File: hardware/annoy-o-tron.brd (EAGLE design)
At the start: 100 x 78.2 mm, 22 parts, among them J1 USB-MICROB, J2 DM3AT-SF-PEJM5, U1 ATMEGA32-16AU, U2 TPS62203DBVT

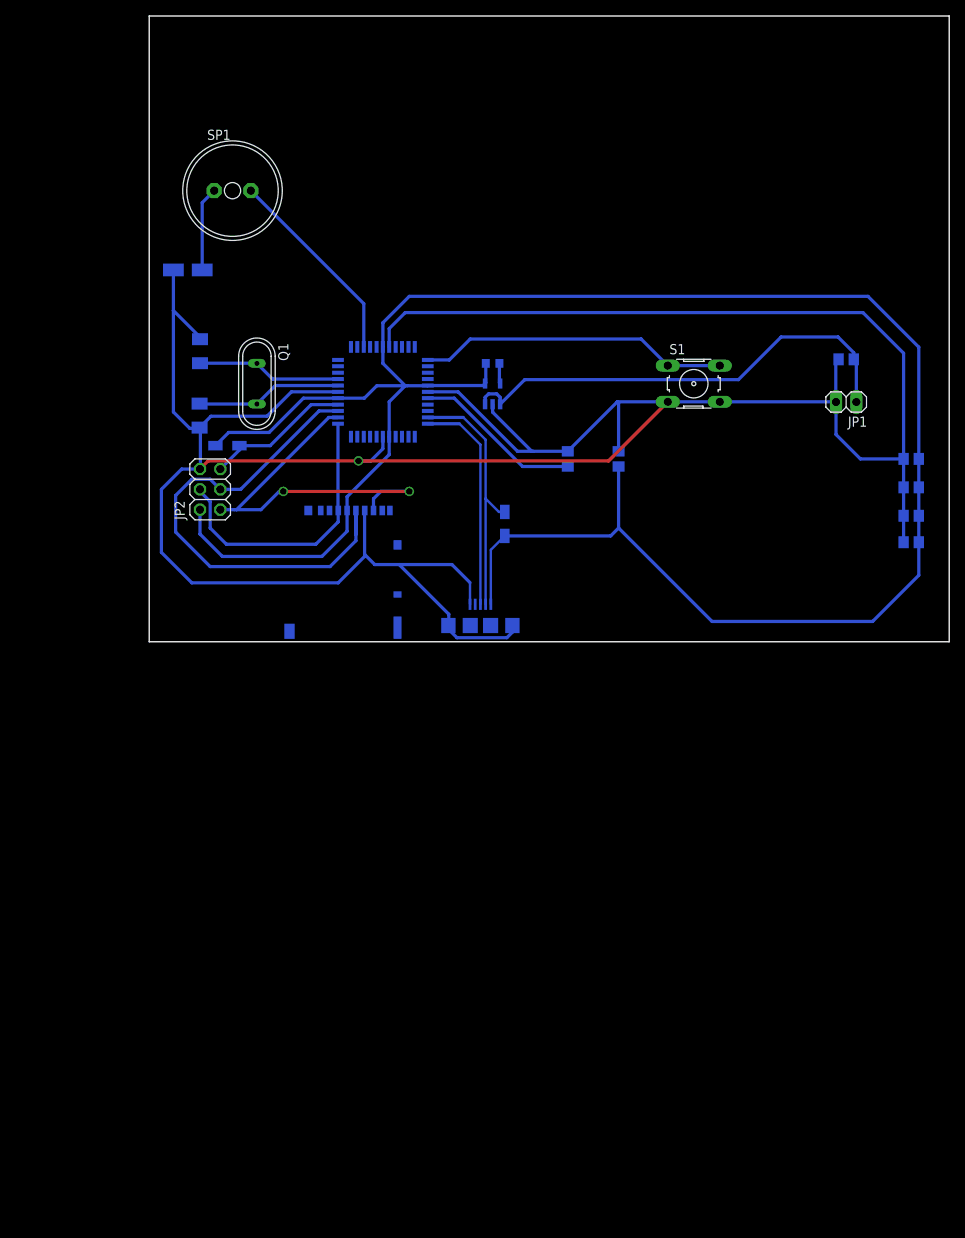
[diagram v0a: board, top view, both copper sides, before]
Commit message: Replaced ATmega32-16 with ATmega328P. Replace TPS62201 with TPS61201, schematic stil unfinished.
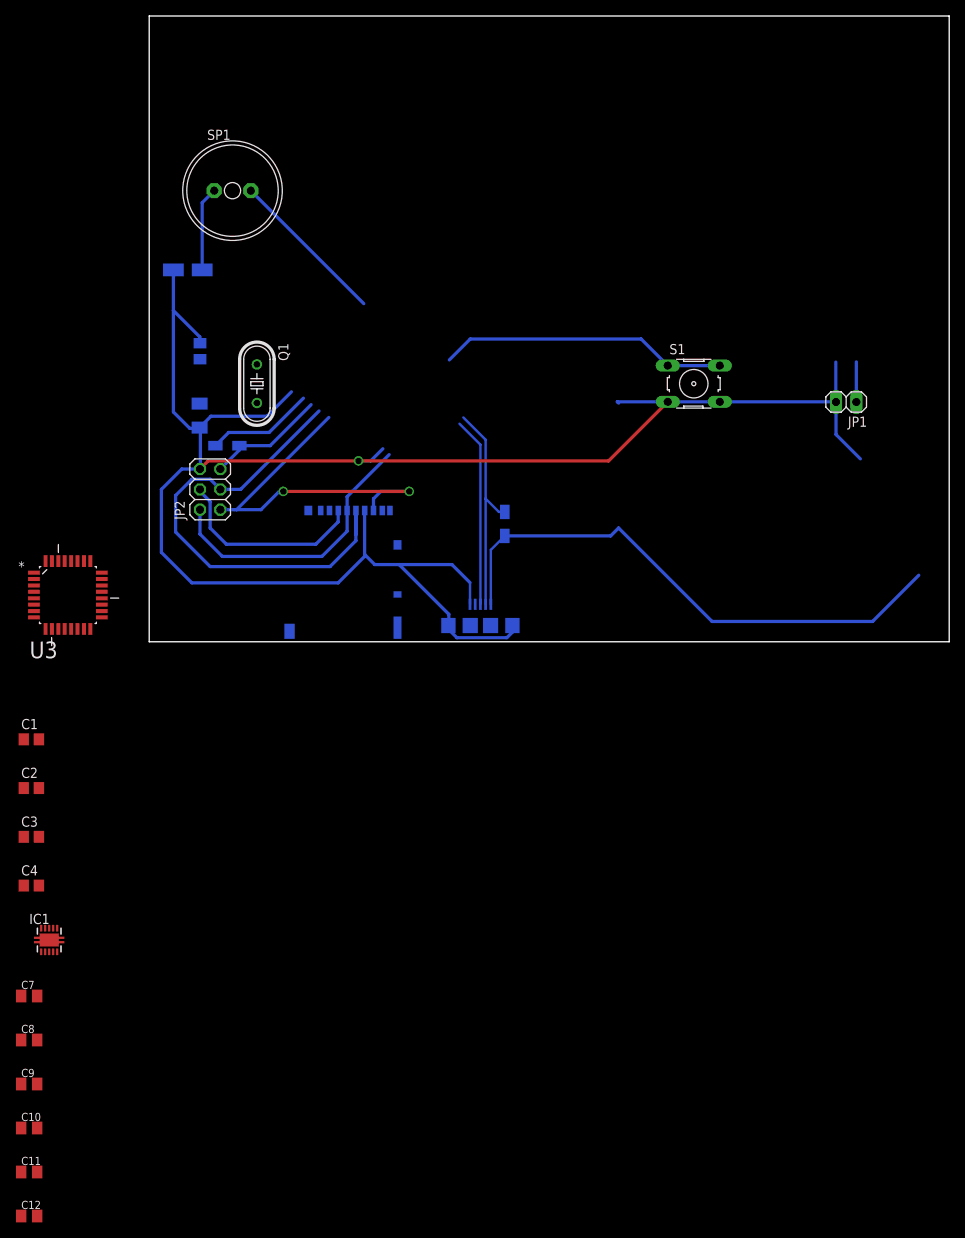
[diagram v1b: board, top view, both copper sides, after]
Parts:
- removed L1: 10uH, rcl:R0603
- removed U1: ATMEGA32-16AU, annoy-o-library:QFP80P1200X1200X120-44N
- removed U2: TPS62203DBVT, annoy-o-library:SOT95P280X145-5N
- added C11: 1uF, resistor:C0805K
- added C12: 100nF, resistor:C0805K
- added C44: 100uF, resistor:153CLV-0405
- added IC1: TPS61201, texas:S-PDSO-N10
- added U3: ATMEGA328P-AU, tudor:QFP80P900X900X120-32N
- C1: value 4.7uF -> 100nF
- C10, C7: value 100nF -> 10uF; device rcl:C0805 -> resistor:C0805K
- C2: value 10uF -> 100nF
- C4: value 100uF -> 100nF; device resistor:153CLV-0405 -> rcl:C0805
- C6: device resistor:C1206K -> resistor:C0805K
- C8, C9: device rcl:C0805 -> resistor:C0805K
- Q1: value (none) -> 8MHz; device special:QS -> crystal:HC49/S
- moved C9 133.1 mm to (-15.0, -53.5), flipped to the top, turned to 0 degrees
- moved C10 132.4 mm to (-15.0, -59.0), flipped to the top, turned to 0 degrees
- moved C7 125.5 mm to (-15.0, -42.5), flipped to the top, turned to 0 degrees
- moved C2 117.4 mm to (-14.7, -16.5), flipped to the top
- moved C1 112.4 mm to (-14.7, -10.4), flipped to the top
- moved C8 103.5 mm to (-15.0, -48.0), flipped to the top, turned to 0 degrees
- moved C3 82.0 mm to (-14.7, -22.6), flipped to the top, turned to 0 degrees
- moved C4 79.4 mm to (-14.7, -28.7), flipped to the top
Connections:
- removed net N$7: SP1.+, U1.14
- new net N$3: C9.1, IC1.1
- new net RESET: U3.29
- new net SPKR: SP1.+, U3.13
- new net SS: U3.14
- new net VCC/2: C7.2, C8.2, IC1.5, IC1.6, IC1.7
- net BUTTON: now also U3.32; no longer U1.23
- net D+: now also U3.23; no longer U1.33
- net D-: now also U3.24; no longer U1.32
- net GND: now also C1.1, C10.2, C11.2, C12.2, C2.1, C4.1, C44.+, C9.2, IC1.4, IC1.8, IC1.9, IC1.PP, IC1.PP@1, IC1.PP@2, U3.21, U3.3, U3.5; no longer C1.2, C10.1, C2.2, C4.+, C9.1, U1.18, U1.28, U1.39, U1.6, U2.2
- net MISO: now also U3.16; no longer U1.2
- net MOSI: now also U3.15; no longer U1.1
- net N$1: now also IC1.3; no longer L1.1, U2.5
- net N$2: now also C1.2, U3.20; no longer C3.2, U1.29
- net N$8: now also C44.-; no longer C4.-
- net RST: no longer U1.4
- net SCK: now also U3.17; no longer U1.3
- net VCC: now also C10.1, C11.1, C12.1, C2.2, C3.2, C4.2, IC1.10, IC1.2, U3.18, U3.4, U3.6; no longer C1.1, U2.1, U2.3
- net VIN: no longer C10.2, C2.1, C7.2, C8.2, C9.2, L1.2, U1.17, U1.27, U1.38, U1.5, U2.4
- net XTAL1: now also Q1.2, U3.7; no longer Q1.1, U1.8
- net XTAL2: now also Q1.1, U3.8; no longer Q1.2, U1.7
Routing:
- net VIN: track 269.9 -> 118.2 mm
- net GND: track 387.6 -> 238.0 mm
- net VCC: track 58.8 -> 5.01 mm
- net N$7: track 25.4 -> 0.00 mm
- net N$2: track 21.0 -> 0.00 mm
- net SPKR: track 0.00 -> 20.0 mm
- net XTAL2: track 18.3 -> 0.00 mm
- net XTAL1: track 18.1 -> 0.00 mm
- net MOSI: track 35.6 -> 24.8 mm
- net D-: track 32.0 -> 27.6 mm
- net D+: track 27.6 -> 23.7 mm
- net RST: track 18.4 -> 15.0 mm
- net BUTTON: track 39.0 -> 36.3 mm
- net N$1: track 2.55 -> 0.00 mm
- net SCK: track 62.8 -> 60.4 mm
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
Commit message: Finished schematic.
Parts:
- removed C44: 100uF, resistor:153CLV-0405
- removed J1: USB-MICROB, SparkFun-Connectors:USB-MICROB
- removed S1: (no value), switch-omron:B3F-10XX
- added C13: 100uF, resistor:153CLV-0405
- added JP3: (no value), pinhead:1X02
- added L1: 2.2uH, tudor:SRN3012TA
- added R3: 10k, rcl:R0805
- C5: device resistor:C1206K -> rcl:C0805K
- JP2: value (none) -> AVR-ISP-6VERT; device pinhead:2X03 -> avr-7:AVR-ISP-6
- R1: device resistor:R1206W -> rcl:R0805
- R2: value 2k2 -> 10k; device resistor:R1206W -> rcl:R0805
- moved C10 106.3 mm to (49.5, 25.5), flipped to the bottom
- moved C11 106.3 mm to (49.5, 20.0), flipped to the bottom
- moved C12 106.3 mm to (49.5, 14.5), flipped to the bottom
- moved C7 106.3 mm to (49.5, 42.0), flipped to the bottom
- moved C8 106.3 mm to (49.5, 36.5), flipped to the bottom
- moved C9 106.3 mm to (49.5, 31.0), flipped to the bottom
- moved C1 106.0 mm to (49.2, 74.1), flipped to the bottom
- moved C2 106.0 mm to (49.2, 68.0), flipped to the bottom
- moved C3 106.0 mm to (49.2, 61.9), flipped to the bottom
- moved C4 106.0 mm to (49.2, 55.8), flipped to the bottom
- moved IC1 103.3 mm to (47.0, 49.0), flipped to the bottom
- moved U3 93.5 mm to (83.3, 10.6), flipped to the bottom
- moved R2 12.1 mm to (53.5, 8.50), turned to 0 degrees
- moved C5 2.00 mm to (6.30, 28.0)
- moved C6 2.00 mm to (6.35, 36.1)
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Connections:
- removed net D+: J1.D+, U3.23
- removed net D-: J1.D-, R2.1, U3.24
- removed net N$8: C44.-, SP1.-
- removed net RST: JP2.5, R1.2
- removed net VIN: J1.VBUS, J2.4, JP2.2, R1.1, R2.2
- new net INS: J2.B, R2.2, U3.12
- new net N$4: C13.+, SP1.-
- net BUTTON: now also JP3.1, R3.2; no longer S1.1, S1.2
- net GND: now also C1.2, C13.-, C2.2, C3.2, C4.2, C7.2, C8.2, JP1.1, R2.1, R3.1; no longer C1.1, C2.1, C3.1, C4.1, C44.+, C7.1, C8.1, J1.GND, J1.MT1, J1.MT2, JP1.2, S1.3, S1.4
- net N$1: now also L1.P$1
- net N$2: now also C1.1; no longer C1.2
- net RESET: now also JP2.5, R1.1
- net SS: now also J2.2
- net VCC: now also C2.1, C3.1, C4.1, J2.4, J2.A, JP2.2, JP3.2, R1.2; no longer C2.2, C3.2, C4.2, JP1.1
- net VCC/2: now also C7.1, C8.1, JP1.2, L1.P$2; no longer C7.2, C8.2
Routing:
- net GND: track 238.0 -> 0.00 mm, vias 1 -> 0
- net VIN: track 118.2 -> 0.00 mm
- net SCK: track 60.4 -> 0.00 mm
- net MISO: track 47.2 -> 0.00 mm, vias 2 -> 0
- net BUTTON: track 36.3 -> 0.00 mm
- net D-: track 27.6 -> 0.00 mm
- net MOSI: track 24.8 -> 0.00 mm
- net D+: track 23.7 -> 0.00 mm
- net SPKR: track 20.0 -> 0.00 mm
- net RST: track 15.0 -> 0.00 mm
- net N$8: track 10.5 -> 0.00 mm
- net VCC: track 5.01 -> 0.00 mm
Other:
- board size 100 x 78.2 mm -> 100 x 78 mm

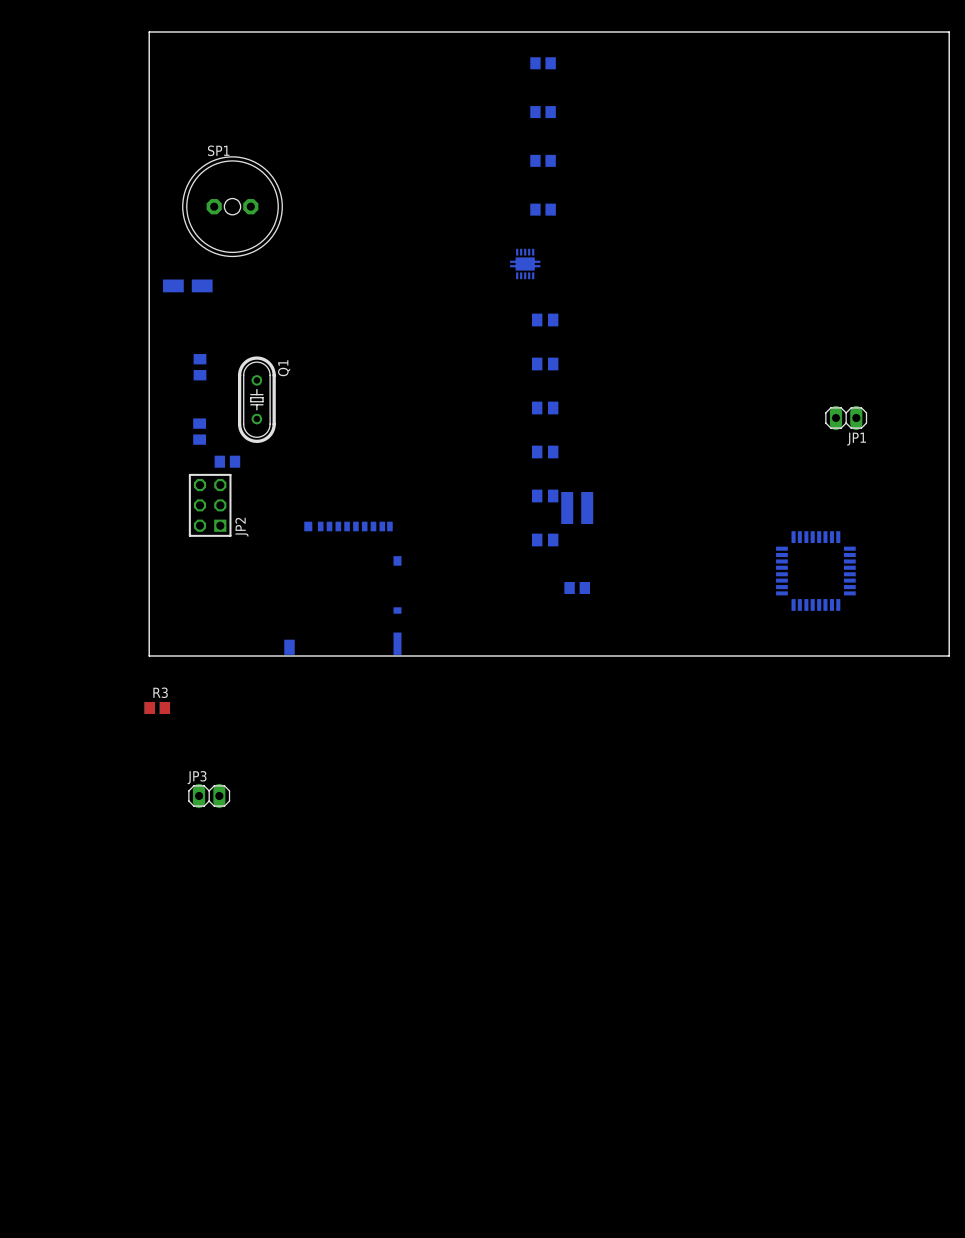
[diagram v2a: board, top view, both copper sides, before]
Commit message: Modifications to schematic. Finished board. Added part list and hardware README.
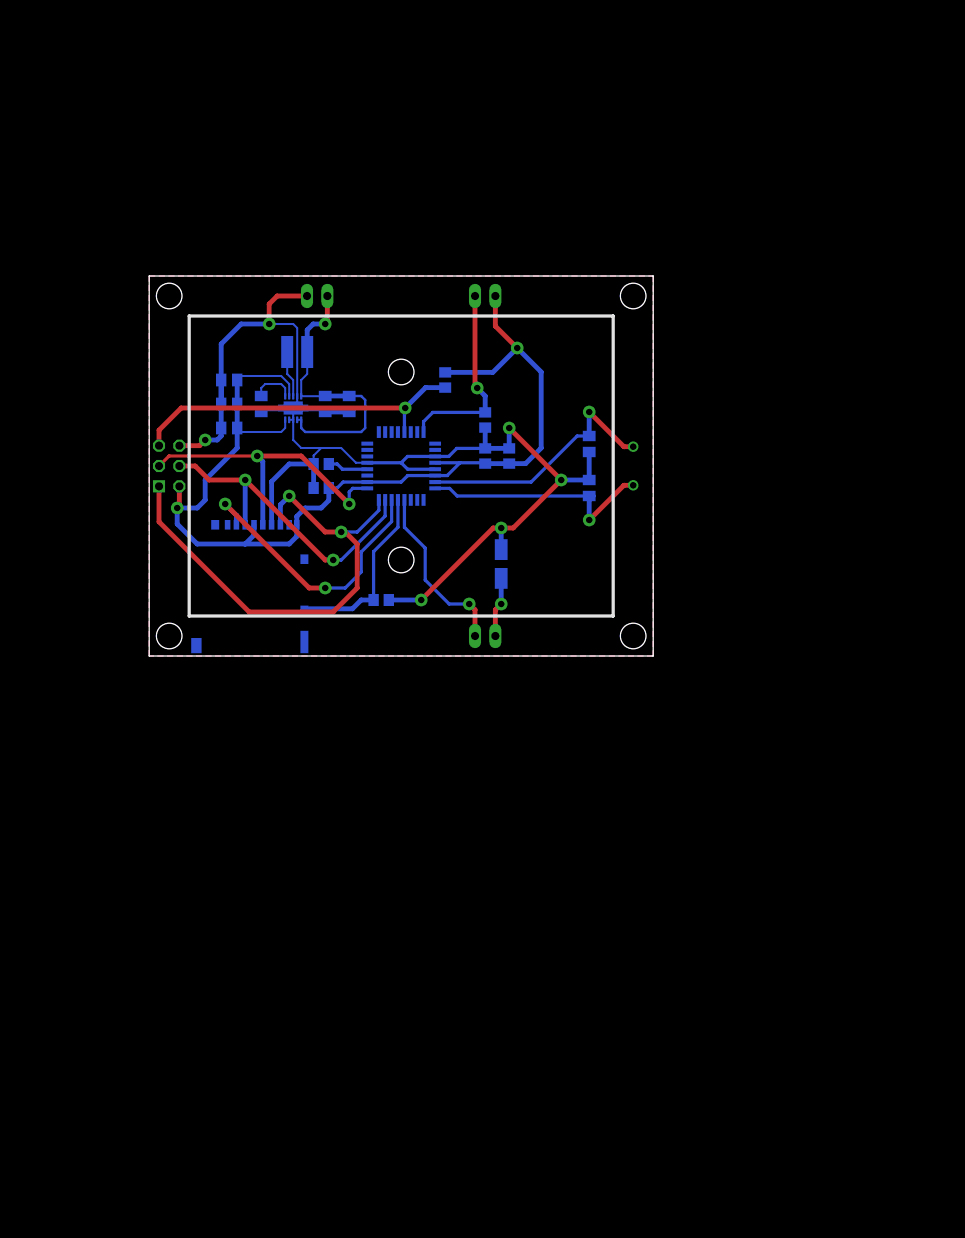
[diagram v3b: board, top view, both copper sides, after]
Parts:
- removed SP1: AL11P, buzzer:AL11P
- added JP4: (no value), pinhead:1X02
- moved JP3 71.4 mm to (42.0, 45.0), flipped to the bottom, turned to 180 degrees
- moved JP1 67.9 mm to (21.0, 45.0), flipped to the bottom
- moved C1 57.3 mm to (21.5, 24.0)
- moved R3 54.6 mm to (42.0, 29.5), flipped to the bottom, turned to 90 degrees
- moved U3 53.5 mm to (31.5, 23.8)
- moved C13 52.4 mm to (44.0, 11.5), turned to 270 degrees
- moved C6 49.6 mm to (55.0, 26.5), turned to 90 degrees
- moved C5 49.2 mm to (55.0, 21.0), turned to 270 degrees
- moved Q1 47.8 mm to (60.5, 23.8), flipped to the bottom, turned to 90 degrees
- moved C4 44.5 mm to (21.5, 21.0)
- moved C2 43.2 mm to (45.0, 25.0), turned to 90 degrees
- moved C12 41.9 mm to (10.0, 28.5)
- moved C11 41.1 mm to (10.0, 31.5)
- moved C10 40.5 mm to (10.0, 34.5)
- moved L1 40.1 mm to (18.5, 38.0), turned to 180 degrees
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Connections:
- net INS: now also J2.A, U3.13; no longer J2.B, U3.12
- net N$4: now also JP4.1; no longer SP1.-
- net SPKR: now also JP4.2, U3.12; no longer SP1.+, U3.13
- net VCC: now also J2.B; no longer J2.A
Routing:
- net GND: track 0.00 -> 166.2 mm, vias 0 -> 6
- net VCC: track 0.00 -> 133.1 mm, vias 0 -> 2
- net MISO: track 0.00 -> 62.8 mm, vias 0 -> 2
- net RESET: track 0.00 -> 43.0 mm, vias 0 -> 1
- net MOSI: track 0.00 -> 40.5 mm, vias 0 -> 2
- net SCK: track 0.00 -> 39.6 mm, vias 0 -> 2
- net VCC/2: track 0.00 -> 36.4 mm, vias 0 -> 1
- net SS: track 0.00 -> 35.9 mm, vias 0 -> 2
- net XTAL1: track 0.00 -> 31.9 mm, vias 0 -> 1
- net XTAL2: track 0.00 -> 31.2 mm, vias 0 -> 1
- net BUTTON: track 0.00 -> 24.6 mm, vias 0 -> 1
- net INS: track 0.00 -> 22.9 mm
- net SPKR: track 0.00 -> 22.1 mm, vias 0 -> 1
- net N$4: track 0.00 -> 7.50 mm, vias 0 -> 1
- net N$1: track 0.00 -> 5.84 mm
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- added copper zone on layer 1, net GND
- added copper zone on layer 16, net GND
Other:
- board size 100 x 78 mm -> 63 x 47.5 mm

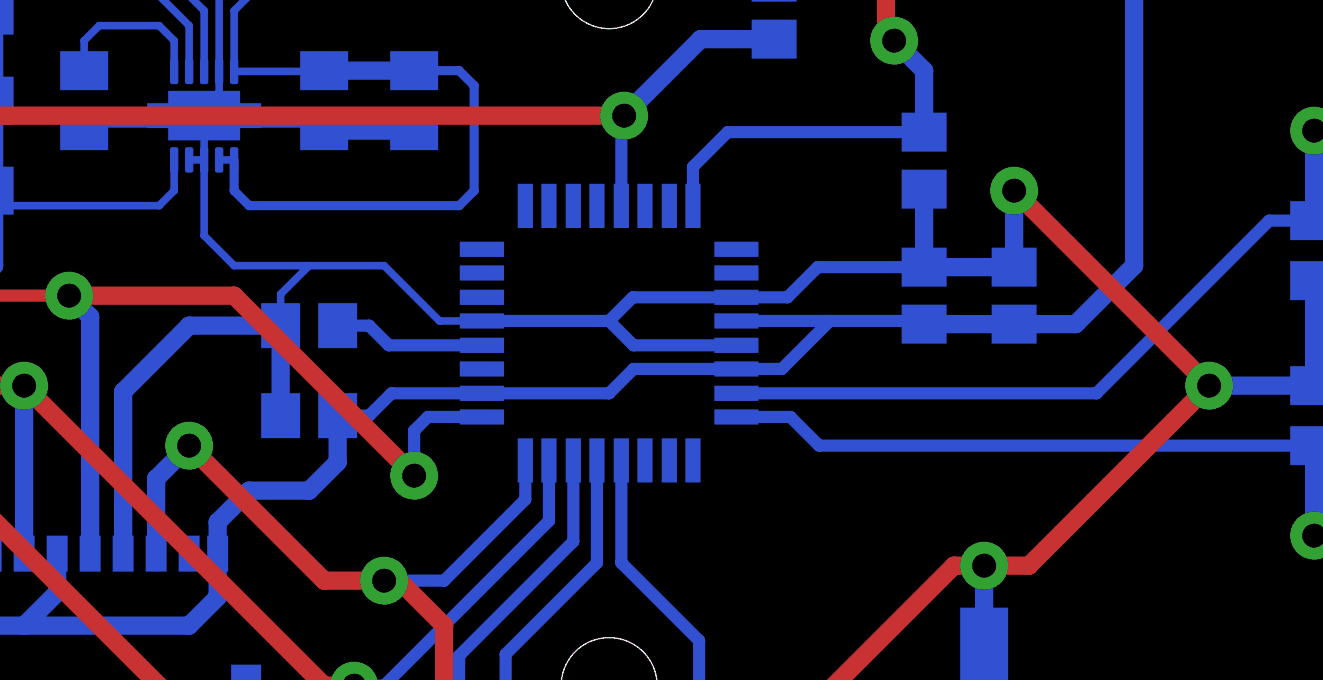
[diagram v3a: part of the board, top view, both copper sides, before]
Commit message: Made capacitor packages uniform. Naming changes in schematic. Board corrections for new packages.
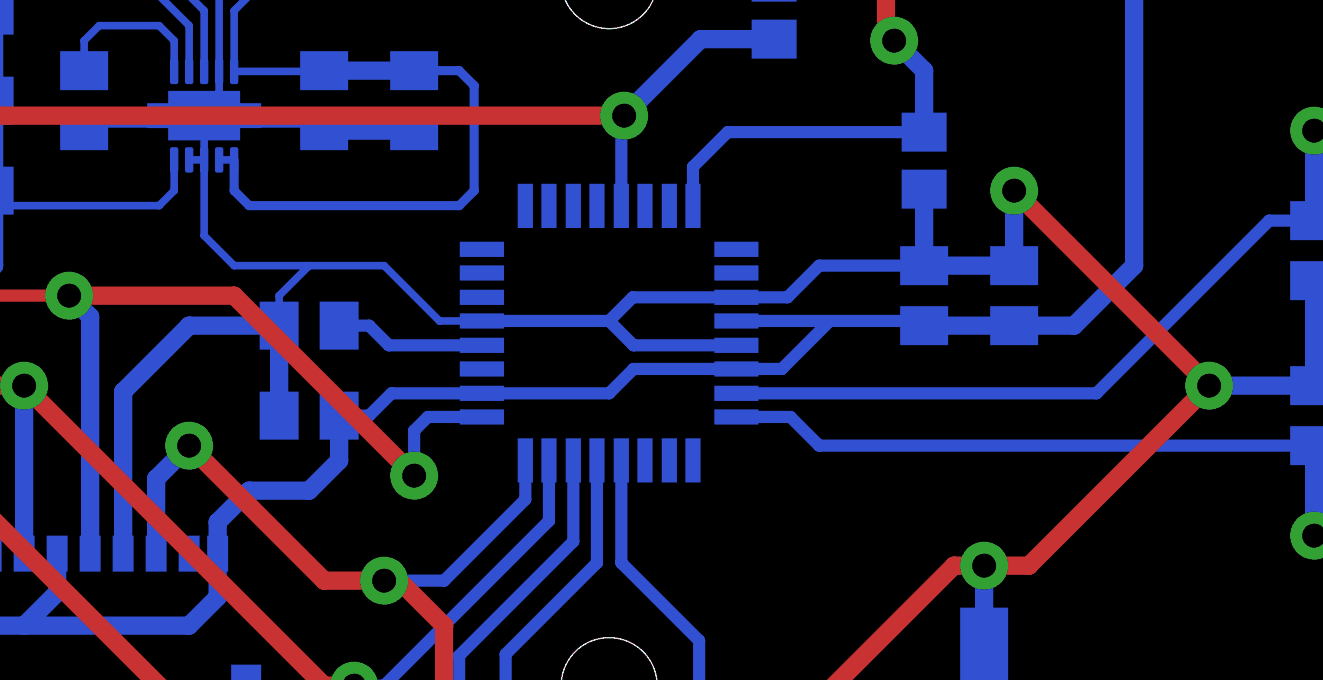
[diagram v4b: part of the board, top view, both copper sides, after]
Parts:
- C1, C2, C3, C4: device rcl:C0805 -> rcl:C0805K
- C10, C11, C12, C6, C7, C8, C9: device resistor:C0805K -> rcl:C0805K
- C13: device resistor:153CLV-0405 -> rcl:153CLV-0405
- renumbered J2 to J1, U3 to U1
